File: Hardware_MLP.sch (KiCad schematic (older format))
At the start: 0 parts

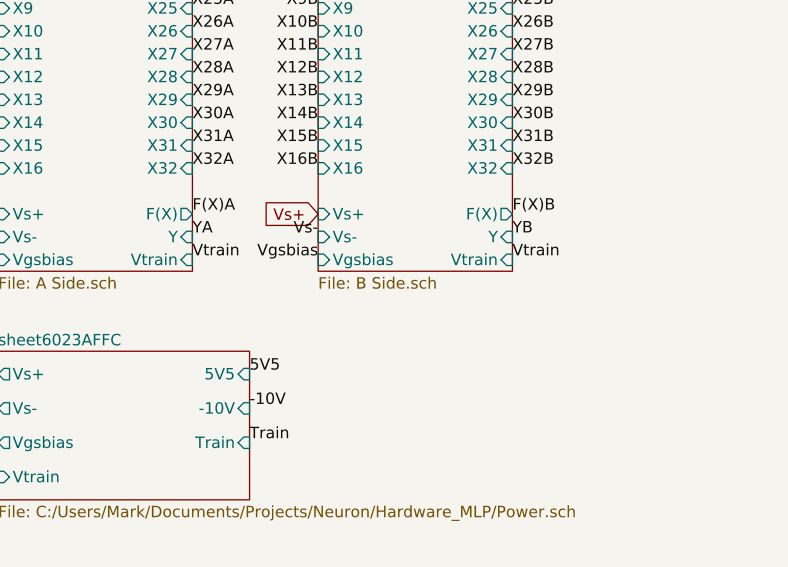
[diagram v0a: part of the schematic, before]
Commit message: Likely Final Component Values
Most values for components that are not dependent on synapse number have been selected.
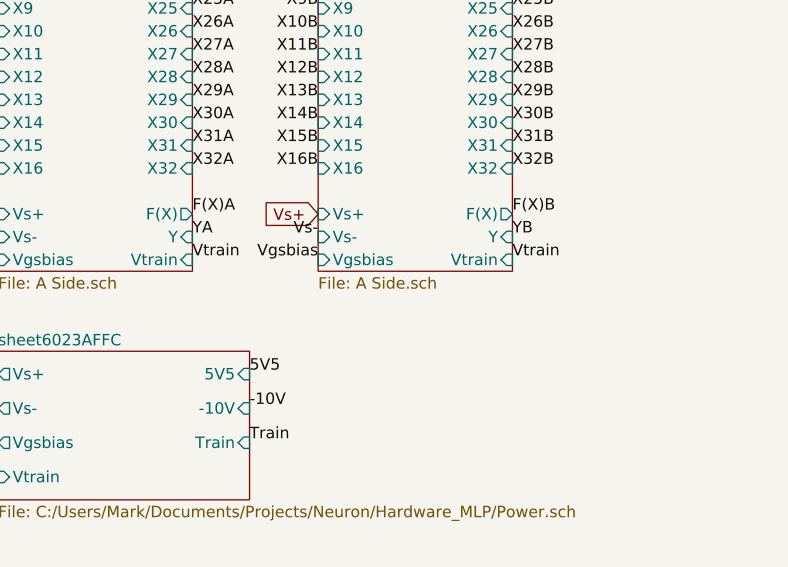
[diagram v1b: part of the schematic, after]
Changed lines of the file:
@@
 U 6024655D
 F0 "B Side" 50
-F1 "B Side.sch" 50
+F1 "A Side.sch" 50
 F2 "X1" I L 7400 2750 50
 F3 "X2" I L 7400 2850 50
